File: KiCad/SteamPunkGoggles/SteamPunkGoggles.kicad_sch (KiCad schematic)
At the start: 6 parts

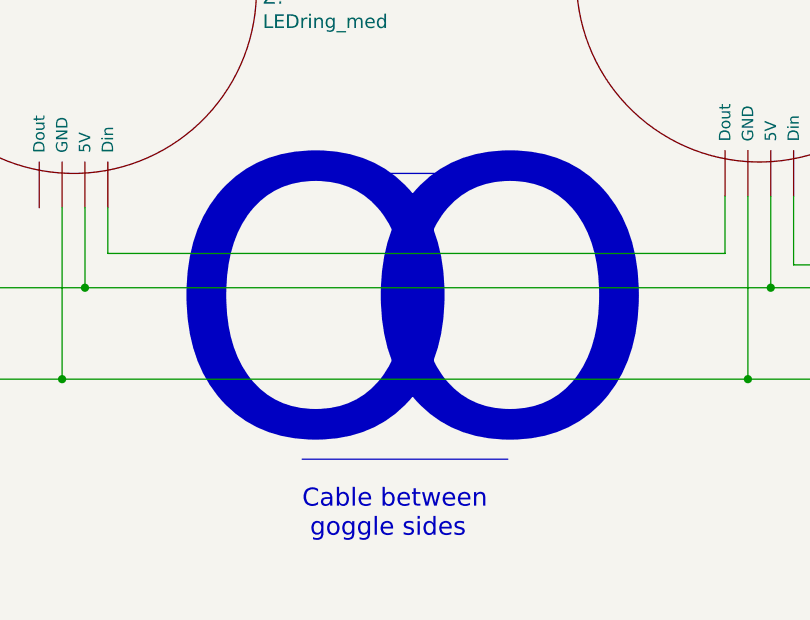
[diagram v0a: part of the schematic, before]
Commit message: minor touch-up for KiCad V7.x
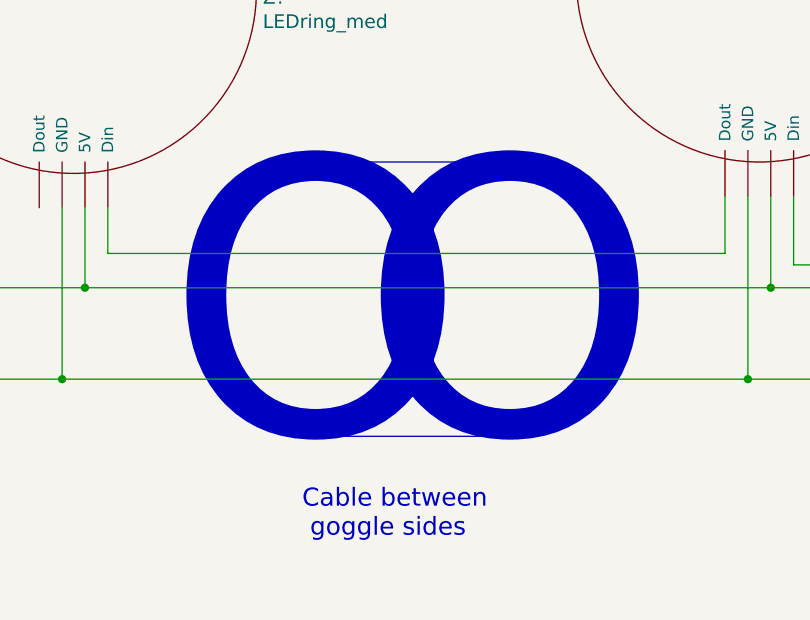
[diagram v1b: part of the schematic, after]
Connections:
- net at A?.~ (VIN): now also Z?.~ (GND)
- net at Z?.~ (GND), Z?.~ (GND): no longer A?.~ (VIN), RV?.1
- new net: A?.~ (VIN), RV?.1, Z?.~ (GND), Z?.~ (GND)
- new net: A?.~ (VIN), Z?.~ (GND), Z?.~ (GND)
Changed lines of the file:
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@@
     (stroke (width 0) (type default))
   )
-  (bus (pts (xy 110.49 110.49) (xy 133.35 110.49))
+  (bus (pts (xy 110.49 109.22) (xy 133.35 109.22))
     (stroke (width 0) (type default))
   )
@@
     (stroke (width 0) (type default))
   )
-  (bus (pts (xy 110.49 142.24) (xy 133.35 142.24))
+  (bus (pts (xy 110.49 139.7) (xy 133.35 139.7))
     (stroke (width 0) (type default))
   )
